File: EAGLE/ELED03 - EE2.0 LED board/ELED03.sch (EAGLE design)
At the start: 18 parts

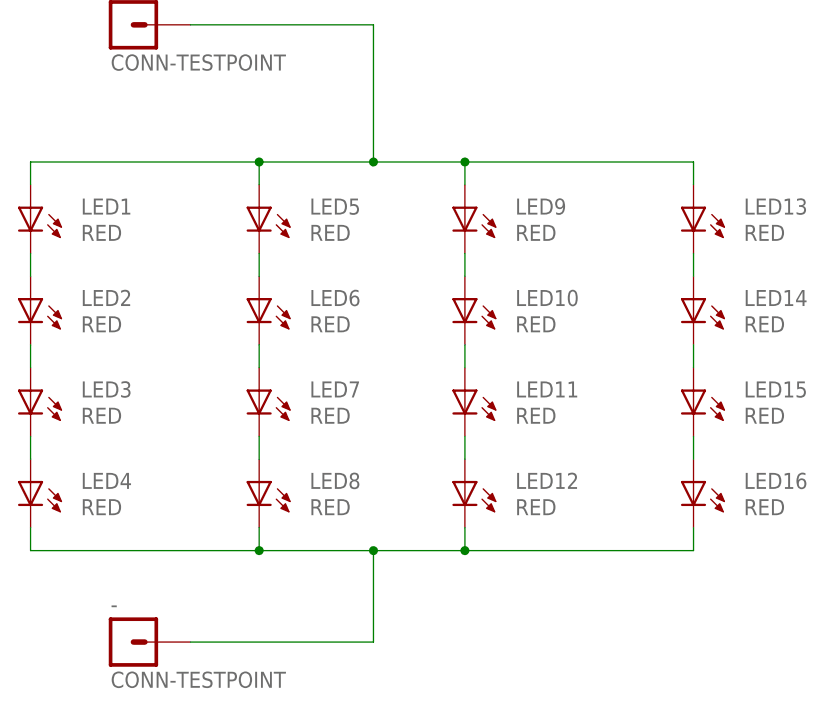
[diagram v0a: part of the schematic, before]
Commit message: On the two ring light boards, I changed the LEDs from 1206 package to 1210 in order to accomodate a brighter LED.
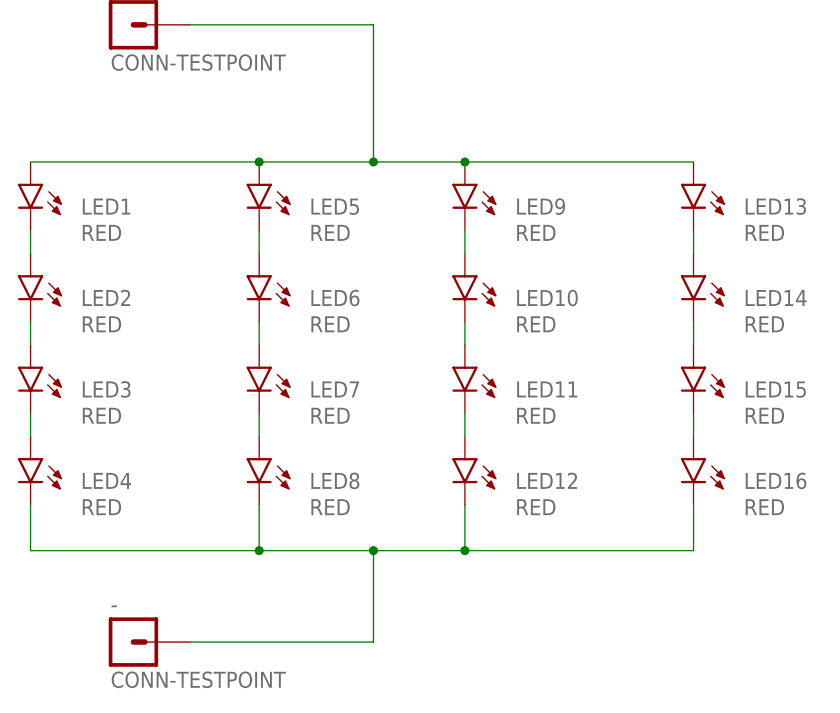
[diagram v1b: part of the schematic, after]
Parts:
- LED1, LED10, LED11, LED12, LED13, LED14, LED15, LED16, LED2, LED3, LED4, LED5, LED6, LED7, LED8, LED9: device SparkFun-LED:LED1206-NS -> GinWhiskers - temp stuff:LED1210
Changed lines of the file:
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@@
 </classes>
 <parts>
-<part name="LED1" library="SparkFun-LED" deviceset="LED" device="1206-NS" value="RED">
-<attribute name="PARTNO" value="LTST-C150CKT"/>
-</part>
-<part name="LED2" library="SparkFun-LED" deviceset="LED" device="1206-NS" value="RED">
-<attribute name="PARTNO" value="LTST-C150CKT"/>
-</part>
-<part name="LED3" library="SparkFun-LED" deviceset="LED" device="1206-NS" value="RED">
-<attribute name="PARTNO" value="LTST-C150CKT"/>
-</part>
-<part name="LED4" library="SparkFun-LED" deviceset="LED" device="1206-NS" value="RED">
-<attribute name="PARTNO" value="LTST-C150CKT"/>
-</part>
-<part name="LED5" library="SparkFun-LED" deviceset="LED" device="1206-NS" value="RED">
-<attribute name="PARTNO" value="LTST-C150CKT"/>
-</part>
-<part name="LED6" library="SparkFun-LED" deviceset="LED" device="1206-NS" value="RED">
-<attribute name="PARTNO" value="LTST-C150CKT"/>
-</part>
-<part name="LED7" library="SparkFun-LED" deviceset="LED" device="1206-NS" value="RED">
-<attribute name="PARTNO" value="LTST-C150CKT"/>
-</part>
-<part name="LED8" library="SparkFun-LED" deviceset="LED" device="1206-NS" value="RED">
-<attribute name="PARTNO" value="LTST-C150CKT"/>
-</part>
-<part name="LED9" library="SparkFun-LED" deviceset="LED" device="1206-NS" value="RED">
-<attribute name="PARTNO" value="LTST-C150CKT"/>
-</part>
-<part name="LED10" library="SparkFun-LED" deviceset="LED" device="1206-NS" value="RED">
-<attribute name="PARTNO" value="LTST-C150CKT"/>
-</part>
-<part name="LED11" library="SparkFun-LED" deviceset="LED" device="1206-NS" value="RED">
-<attribute name="PARTNO" value="LTST-C150CKT"/>
-</part>
-<part name="LED12" library="SparkFun-LED" deviceset="LED" device="1206-NS" value="RED">
-<attribute name="PARTNO" value="LTST-C150CKT"/>
-</part>
-<part name="LED13" library="SparkFun-LED" deviceset="LED" device="1206-NS" value="RED">
-<attribute name="PARTNO" value="LTST-C150CKT"/>
-</part>
-<part name="LED14" library="SparkFun-LED" deviceset="LED" device="1206-NS" value="RED">
-<attribute name="PARTNO" value="LTST-C150CKT"/>
-</part>
-<part name="LED15" library="SparkFun-LED" deviceset="LED" device="1206-NS" value="RED">
-<attribute name="PARTNO" value="LTST-C150CKT"/>
-</part>
-<part name="LED16" library="SparkFun-LED" deviceset="LED" device="1206-NS" value="RED">
+<part name="LED1" library="GinWhiskers - temp stuff" deviceset="LED" device="1210" value="RED">
+<attribute name="PARTNO" value="LTST-C150CKT"/>
+</part>
+<part name="LED2" library="GinWhiskers - temp stuff" deviceset="LED" device="1210" value="RED">
+<attribute name="PARTNO" value="LTST-C150CKT"/>
+</part>
+<part name="LED3" library="GinWhiskers - temp stuff" deviceset="LED" device="1210" value="RED">
+<attribute name="PARTNO" value="LTST-C150CKT"/>
+</part>
+<part name="LED4" library="GinWhiskers - temp stuff" deviceset="LED" device="1210" value="RED">
+<attribute name="PARTNO" value="LTST-C150CKT"/>
+</part>
+<part name="LED5" library="GinWhiskers - temp stuff" deviceset="LED" device="1210" value="RED">
+<attribute name="PARTNO" value="LTST-C150CKT"/>
+</part>
+<part name="LED6" library="GinWhiskers - temp stuff" deviceset="LED" device="1210" value="RED">
+<attribute name="PARTNO" value="LTST-C150CKT"/>
+</part>
+<part name="LED7" library="GinWhiskers - temp stuff" deviceset="LED" device="1210" value="RED">
+<attribute name="PARTNO" value="LTST-C150CKT"/>
+</part>
+<part name="LED8" library="GinWhiskers - temp stuff" deviceset="LED" device="1210" value="RED">
+<attribute name="PARTNO" value="LTST-C150CKT"/>
+</part>
+<part name="LED9" library="GinWhiskers - temp stuff" deviceset="LED" device="1210" value="RED">
+<attribute name="PARTNO" value="LTST-C150CKT"/>
+</part>
+<part name="LED10" library="GinWhiskers - temp stuff" deviceset="LED" device="1210" value="RED">
+<attribute name="PARTNO" value="LTST-C150CKT"/>
+</part>
+<part name="LED11" library="GinWhiskers - temp stuff" deviceset="LED" device="1210" value="RED">
+<attribute name="PARTNO" value="LTST-C150CKT"/>
+</part>
+<part name="LED12" library="GinWhiskers - temp stuff" deviceset="LED" device="1210" value="RED">
+<attribute name="PARTNO" value="LTST-C150CKT"/>
+</part>
+<part name="LED13" library="GinWhiskers - temp stuff" deviceset="LED" device="1210" value="RED">
+<attribute name="PARTNO" value="LTST-C150CKT"/>
+</part>
+<part name="LED14" library="GinWhiskers - temp stuff" deviceset="LED" device="1210" value="RED">
+<attribute name="PARTNO" value="LTST-C150CKT"/>
+</part>
+<part name="LED15" library="GinWhiskers - temp stuff" deviceset="LED" device="1210" value="RED">
+<attribute name="PARTNO" value="LTST-C150CKT"/>
+</part>
+<part name="LED16" library="GinWhiskers - temp stuff" deviceset="LED" device="1210" value="RED">
 <attribute name="PARTNO" value="LTST-C150CKT"/>
 </part>
@@
 <pinref part="LED2" gate="G$1" pin="A"/>
 <pinref part="LED1" gate="G$1" pin="C"/>
-<wire x1="17.78" y1="63.5" x2="17.78" y2="66.04" width="0.1524" layer="91"/>
+<wire x1="17.78" y1="66.04" x2="17.78" y2="68.58" width="0.1524" layer="91"/>
 </segment>
 </net>
@@
 <pinref part="LED2" gate="G$1" pin="C"/>
 <pinref part="LED3" gate="G$1" pin="A"/>
-<wire x1="17.78" y1="55.88" x2="17.78" y2="53.34" width="0.1524" layer="91"/>
+<wire x1="17.78" y1="58.42" x2="17.78" y2="55.88" width="0.1524" layer="91"/>
 </segment>
 </net>
@@
 <pinref part="LED4" gate="G$1" pin="A"/>
 <pinref part="LED3" gate="G$1" pin="C"/>
-<wire x1="17.78" y1="43.18" x2="17.78" y2="45.72" width="0.1524" layer="91"/>
+<wire x1="17.78" y1="45.72" x2="17.78" y2="48.26" width="0.1524" layer="91"/>
 </segment>
 </net>
@@
 <pinref part="LED8" gate="G$1" pin="A"/>
 <pinref part="LED7" gate="G$1" pin="C"/>
-<wire x1="43.18" y1="43.18" x2="43.18" y2="45.72" width="0.1524" layer="91"/>
+<wire x1="43.18" y1="45.72" x2="43.18" y2="48.26" width="0.1524" layer="91"/>
 </segment>
 </net>
@@
 <pinref part="LED7" gate="G$1" pin="A"/>
 <pinref part="LED6" gate="G$1" pin="C"/>
-<wire x1="43.18" y1="53.34" x2="43.18" y2="55.88" width="0.1524" layer="91"/>
+<wire x1="43.18" y1="55.88" x2="43.18" y2="58.42" width="0.1524" layer="91"/>
 </segment>
 </net>
@@
 <pinref part="LED6" gate="G$1" pin="A"/>
 <pinref part="LED5" gate="G$1" pin="C"/>
-<wire x1="43.18" y1="63.5" x2="43.18" y2="66.04" width="0.1524" layer="91"/>
+<wire x1="43.18" y1="66.04" x2="43.18" y2="68.58" width="0.1524" layer="91"/>
 </segment>
 </net>
@@
 <pinref part="LED10" gate="G$1" pin="A"/>
 <pinref part="LED9" gate="G$1" pin="C"/>
-<wire x1="66.04" y1="63.5" x2="66.04" y2="66.04" width="0.1524" layer="91"/>
+<wire x1="66.04" y1="66.04" x2="66.04" y2="68.58" width="0.1524" layer="91"/>
 </segment>
 </net>
@@
 <pinref part="LED10" gate="G$1" pin="C"/>
 <pinref part="LED11" gate="G$1" pin="A"/>
-<wire x1="66.04" y1="55.88" x2="66.04" y2="53.34" width="0.1524" layer="91"/>
+<wire x1="66.04" y1="58.42" x2="66.04" y2="55.88" width="0.1524" layer="91"/>
 </segment>
 </net>
@@
 <pinref part="LED11" gate="G$1" pin="C"/>
 <pinref part="LED12" gate="G$1" pin="A"/>
-<wire x1="66.04" y1="45.72" x2="66.04" y2="43.18" width="0.1524" layer="91"/>
+<wire x1="66.04" y1="48.26" x2="66.04" y2="45.72" width="0.1524" layer="91"/>
 </segment>
 </net>
@@
 <pinref part="LED16" gate="G$1" pin="A"/>
 <pinref part="LED15" gate="G$1" pin="C"/>
-<wire x1="91.44" y1="43.18" x2="91.44" y2="45.72" width="0.1524" layer="91"/>
+<wire x1="91.44" y1="45.72" x2="91.44" y2="48.26" width="0.1524" layer="91"/>
 </segment>
 </net>
@@
 <pinref part="LED15" gate="G$1" pin="A"/>
 <pinref part="LED14" gate="G$1" pin="C"/>
-<wire x1="91.44" y1="53.34" x2="91.44" y2="55.88" width="0.1524" layer="91"/>
+<wire x1="91.44" y1="55.88" x2="91.44" y2="58.42" width="0.1524" layer="91"/>
 </segment>
 </net>
@@
 <pinref part="LED13" gate="G$1" pin="C"/>
 <pinref part="LED14" gate="G$1" pin="A"/>
-<wire x1="91.44" y1="66.04" x2="91.44" y2="63.5" width="0.1524" layer="91"/>
+<wire x1="91.44" y1="68.58" x2="91.44" y2="66.04" width="0.1524" layer="91"/>
 </segment>
 </net>
@@
 <segment>
 <pinref part="LED4" gate="G$1" pin="C"/>
-<wire x1="17.78" y1="35.56" x2="17.78" y2="33.02" width="0.1524" layer="91"/>
+<wire x1="17.78" y1="38.1" x2="17.78" y2="33.02" width="0.1524" layer="91"/>
 <pinref part="LED16" gate="G$1" pin="C"/>
 <wire x1="17.78" y1="33.02" x2="43.18" y2="33.02" width="0.1524" layer="91"/>
@@
 <wire x1="55.88" y1="33.02" x2="66.04" y2="33.02" width="0.1524" layer="91"/>
 <wire x1="66.04" y1="33.02" x2="91.44" y2="33.02" width="0.1524" layer="91"/>
-<wire x1="91.44" y1="33.02" x2="91.44" y2="35.56" width="0.1524" layer="91"/>
+<wire x1="91.44" y1="33.02" x2="91.44" y2="38.1" width="0.1524" layer="91"/>
 <pinref part="LED12" gate="G$1" pin="C"/>
-<wire x1="66.04" y1="35.56" x2="66.04" y2="33.02" width="0.1524" layer="91"/>
+<wire x1="66.04" y1="38.1" x2="66.04" y2="33.02" width="0.1524" layer="91"/>
 <pinref part="LED8" gate="G$1" pin="C"/>
-<wire x1="43.18" y1="35.56" x2="43.18" y2="33.02" width="0.1524" layer="91"/>
+<wire x1="43.18" y1="38.1" x2="43.18" y2="33.02" width="0.1524" layer="91"/>
 <junction x="43.18" y="33.02"/>
 <junction x="66.04" y="33.02"/>
@@
 <segment>
 <pinref part="LED1" gate="G$1" pin="A"/>
-<wire x1="17.78" y1="73.66" x2="17.78" y2="76.2" width="0.1524" layer="91"/>
 <pinref part="LED13" gate="G$1" pin="A"/>
 <wire x1="17.78" y1="76.2" x2="43.18" y2="76.2" width="0.1524" layer="91"/>
@@
 <wire x1="55.88" y1="76.2" x2="66.04" y2="76.2" width="0.1524" layer="91"/>
 <wire x1="66.04" y1="76.2" x2="91.44" y2="76.2" width="0.1524" layer="91"/>
-<wire x1="91.44" y1="76.2" x2="91.44" y2="73.66" width="0.1524" layer="91"/>
 <pinref part="LED9" gate="G$1" pin="A"/>
-<wire x1="66.04" y1="73.66" x2="66.04" y2="76.2" width="0.1524" layer="91"/>
 <pinref part="LED5" gate="G$1" pin="A"/>
-<wire x1="43.18" y1="73.66" x2="43.18" y2="76.2" width="0.1524" layer="91"/>
 <junction x="66.04" y="76.2"/>
 <junction x="43.18" y="76.2"/>

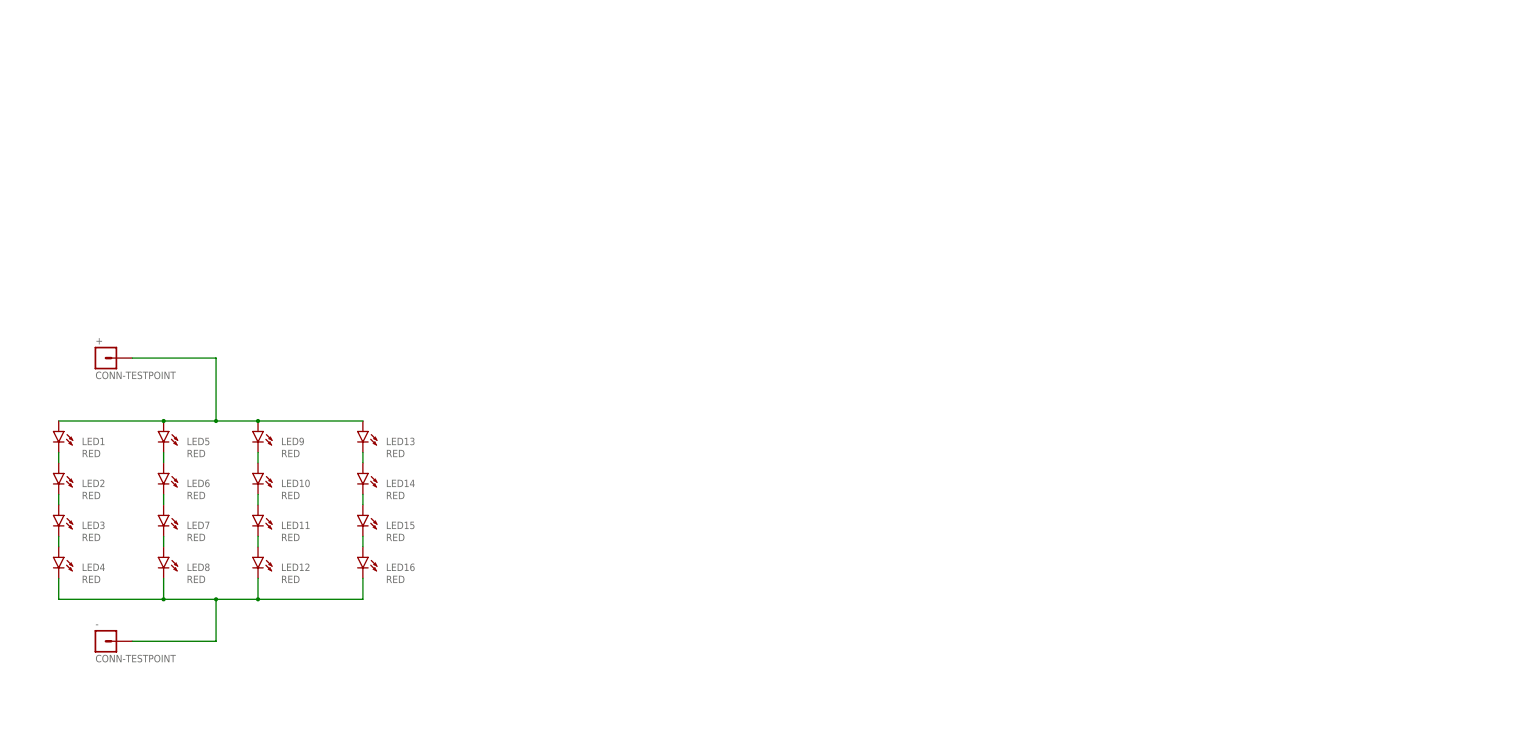
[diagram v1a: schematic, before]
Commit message: Added frames, logos, part numbers, and fiducials
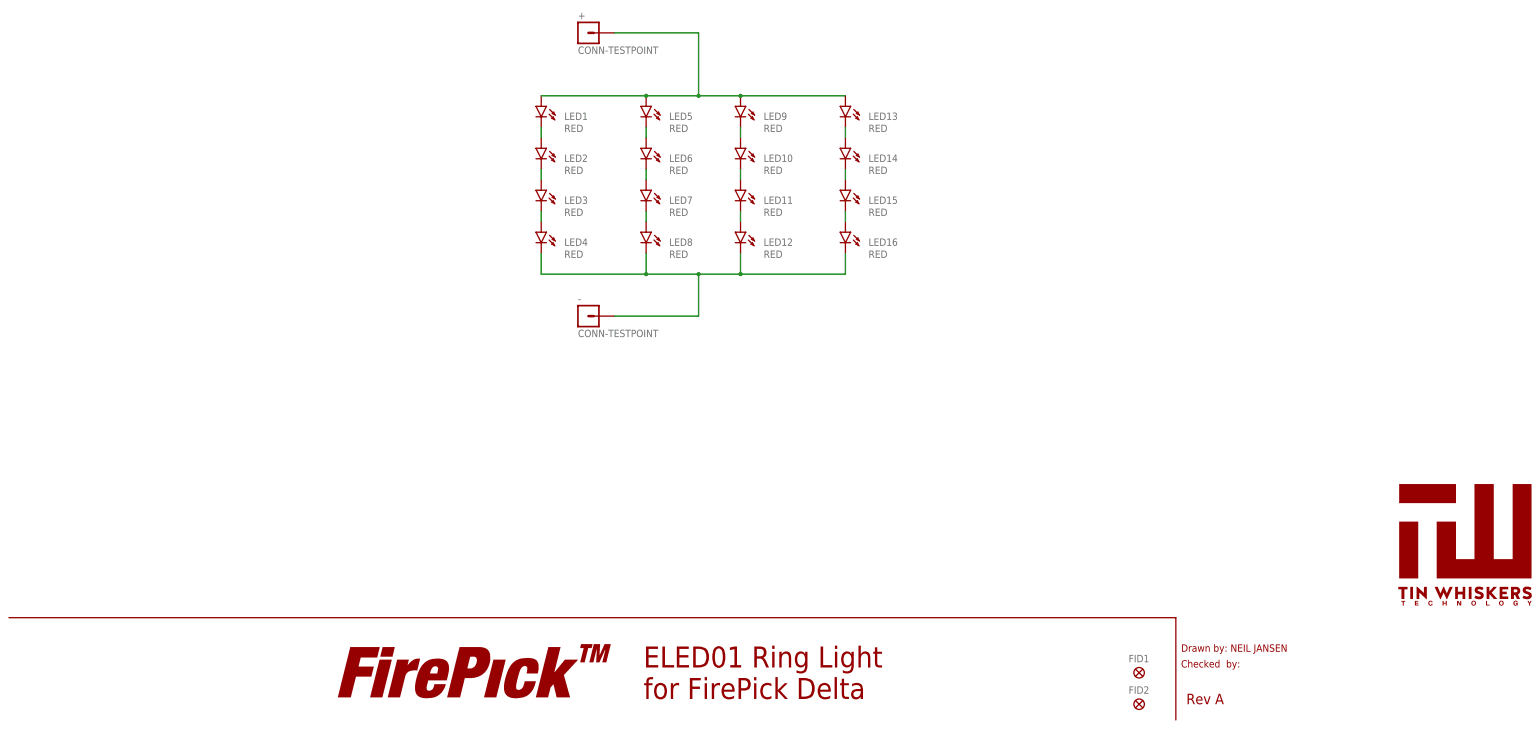
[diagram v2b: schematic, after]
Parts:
- added FID1, FID2: FIDUCIAL, TinWhiskers:FIDUCIAL
- added LOGO4: LOGO-FIREPICKMEDIUM, FirePick:LOGO-FIREPICKMEDIUM
- added U$1: TIN-WHISKERSSMALL, !tin-whiskers-logo:TIN-WHISKERSSMALL
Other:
- note added: "Checked by:"
- note added: "Drawn by: NEIL JANSEN"
- note added: "ELED01 Ring Light for FirePick Delta"
- note added: "Rev A"
- moved on the sheet: +, -, LED1, LED10, LED11, LED12, LED13, LED14, LED15, LED16, LED2, LED3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
